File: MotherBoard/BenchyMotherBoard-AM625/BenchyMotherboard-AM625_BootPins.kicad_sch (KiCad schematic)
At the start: 40 parts, among them U18 74LVC541ABQ,115, U50 74LVC1G08GW,125

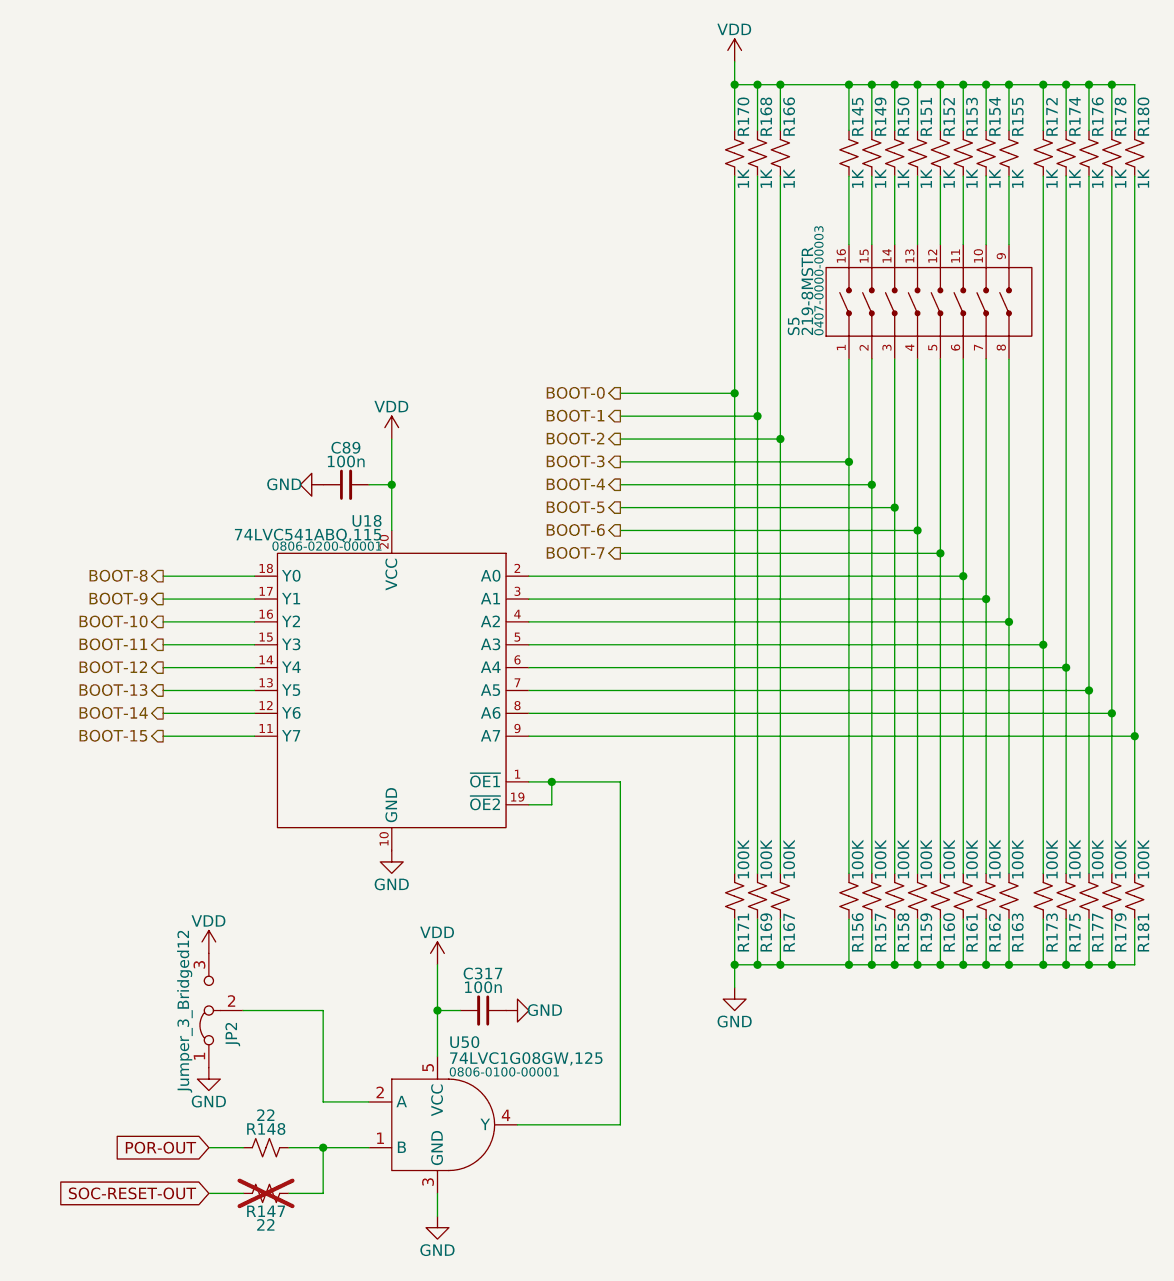
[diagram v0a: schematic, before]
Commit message: Schematic capture mostly complete. Starting PCB layout
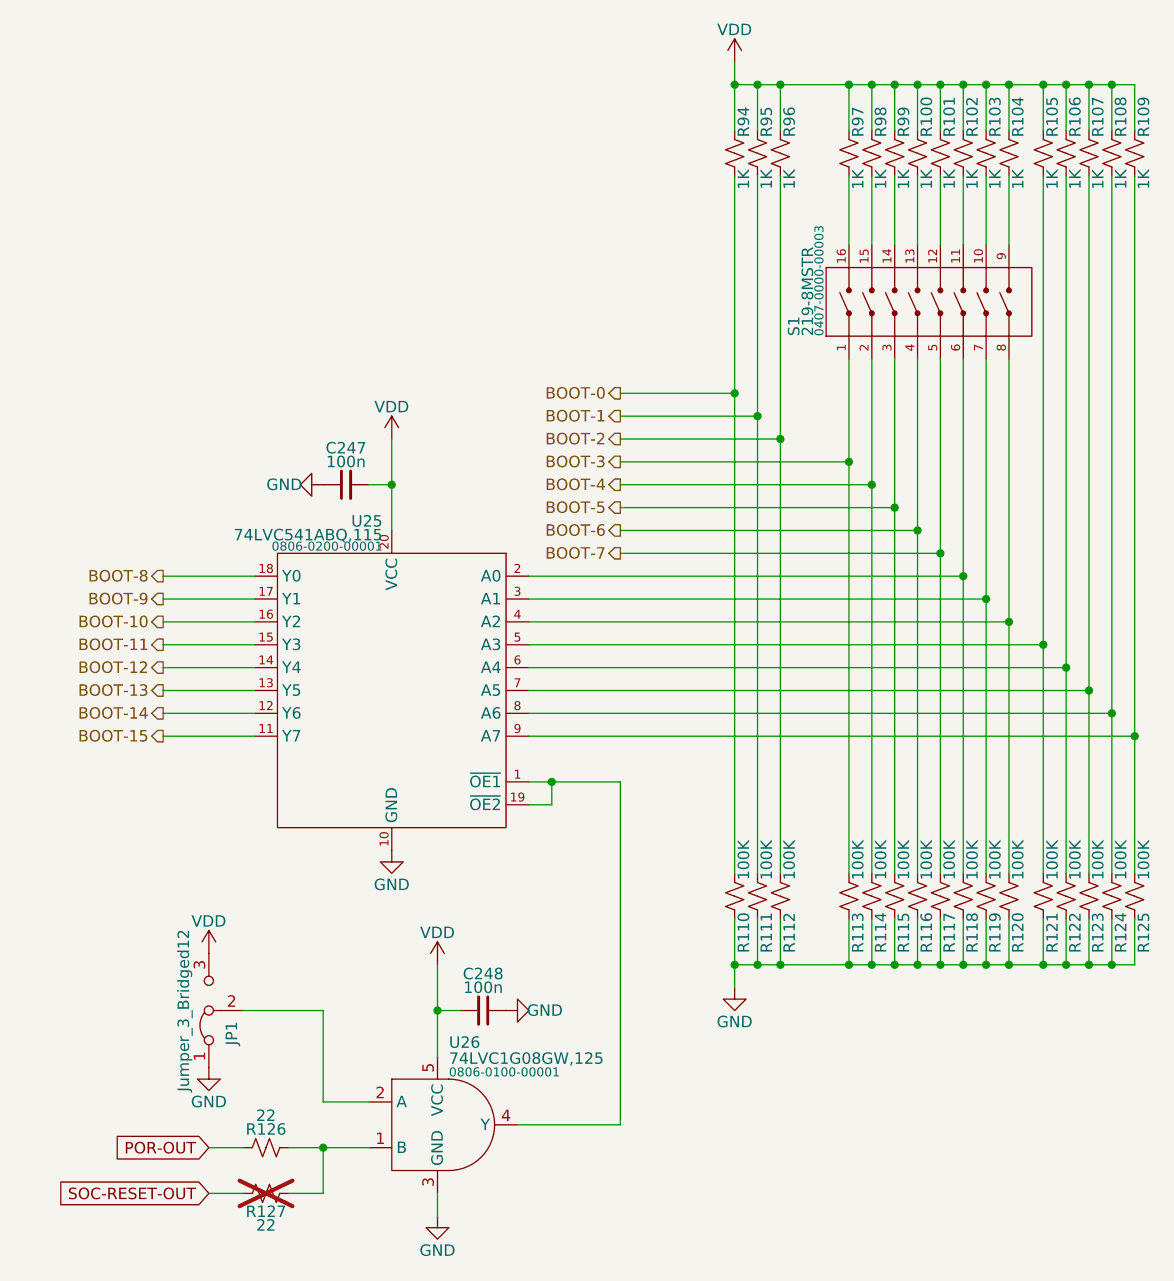
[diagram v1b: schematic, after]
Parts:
- renumbered C89 to C247, C317 to C248, JP2 to JP1, R151 to R100, R152 to R101, R153 to R102, R154 to R103, R155 to R104, R172 to R105, R174 to R106, R176 to R107, R178 to R108, R180 to R109, R171 to R110, R169 to R111, R167 to R112, R156 to R113, R157 to R114, R158 to R115, R159 to R116, R160 to R117, R161 to R118, R162 to R119, R163 to R120, R173 to R121, R175 to R122, R177 to R123, R179 to R124, R181 to R125, R148 to R126, R147 to R127, R170 to R94, R168 to R95, R166 to R96, R145 to R97, R149 to R98, R150 to R99, S5 to S1, U18 to U25, U50 to U26
